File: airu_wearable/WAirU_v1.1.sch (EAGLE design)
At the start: 54 parts, among them Q2 MMBT3904LT1G, Q3 MMBT3904LT1G, Q4 BSS84, Q6 BSS84, U2 CN3065-DFN8, U3 HDC1080DMBT, U4 PAM2305AABADJ, U6 PAM2401, U7 ESP32_WROOM32_SKINNY

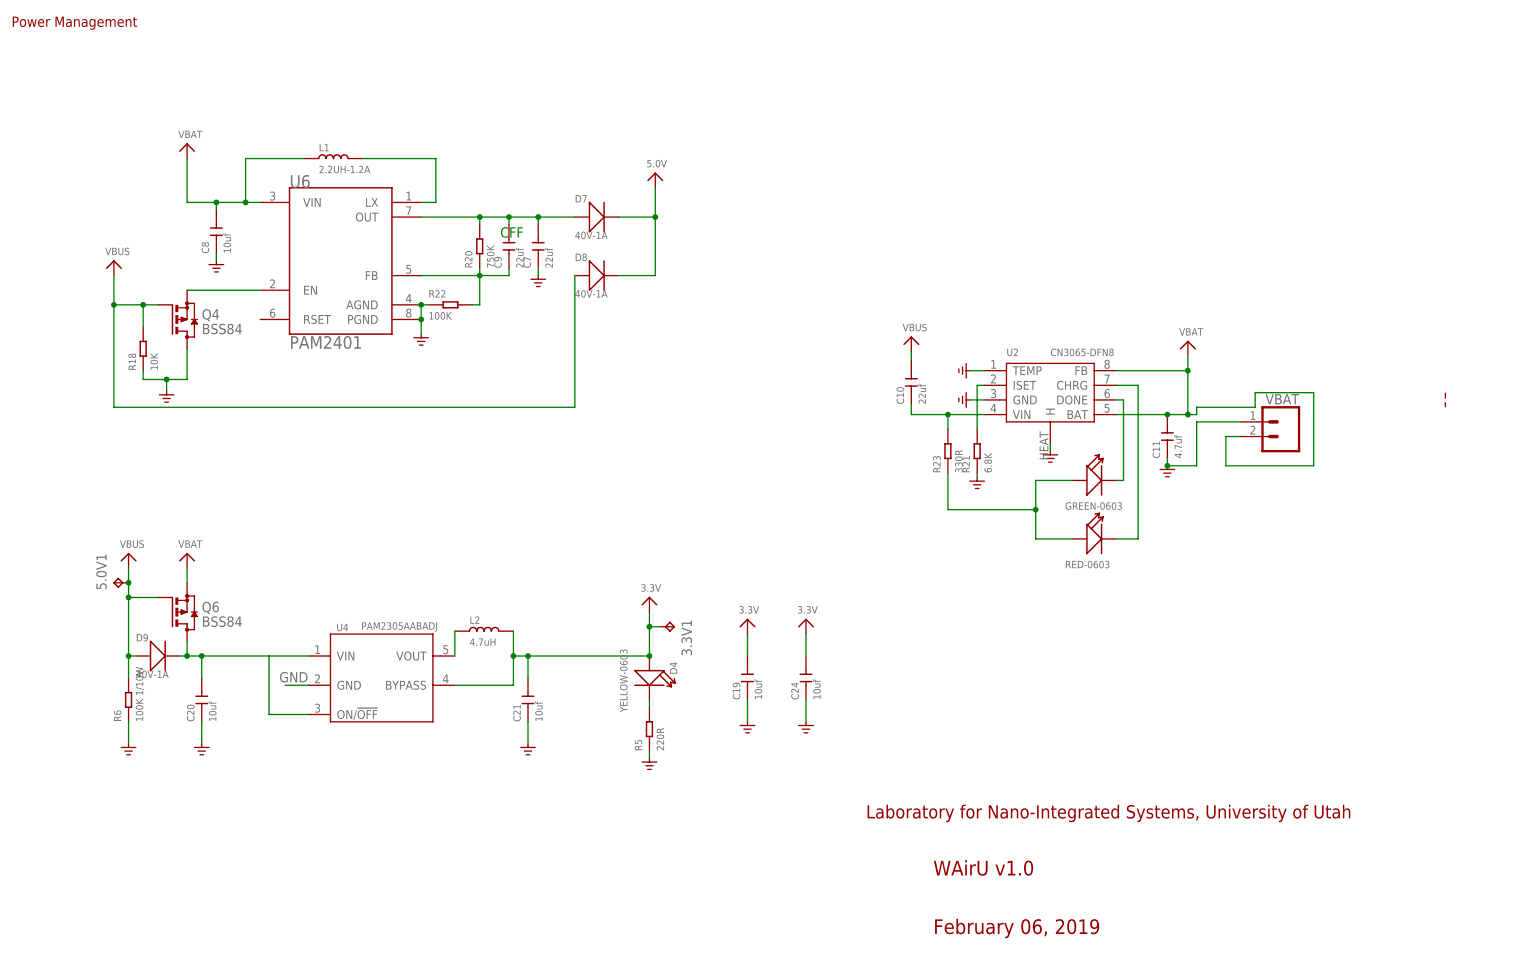
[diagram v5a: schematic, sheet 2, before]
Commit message: replaced LEDs with single LED, 5V and 3.3V buck/boost are now on the same VIN
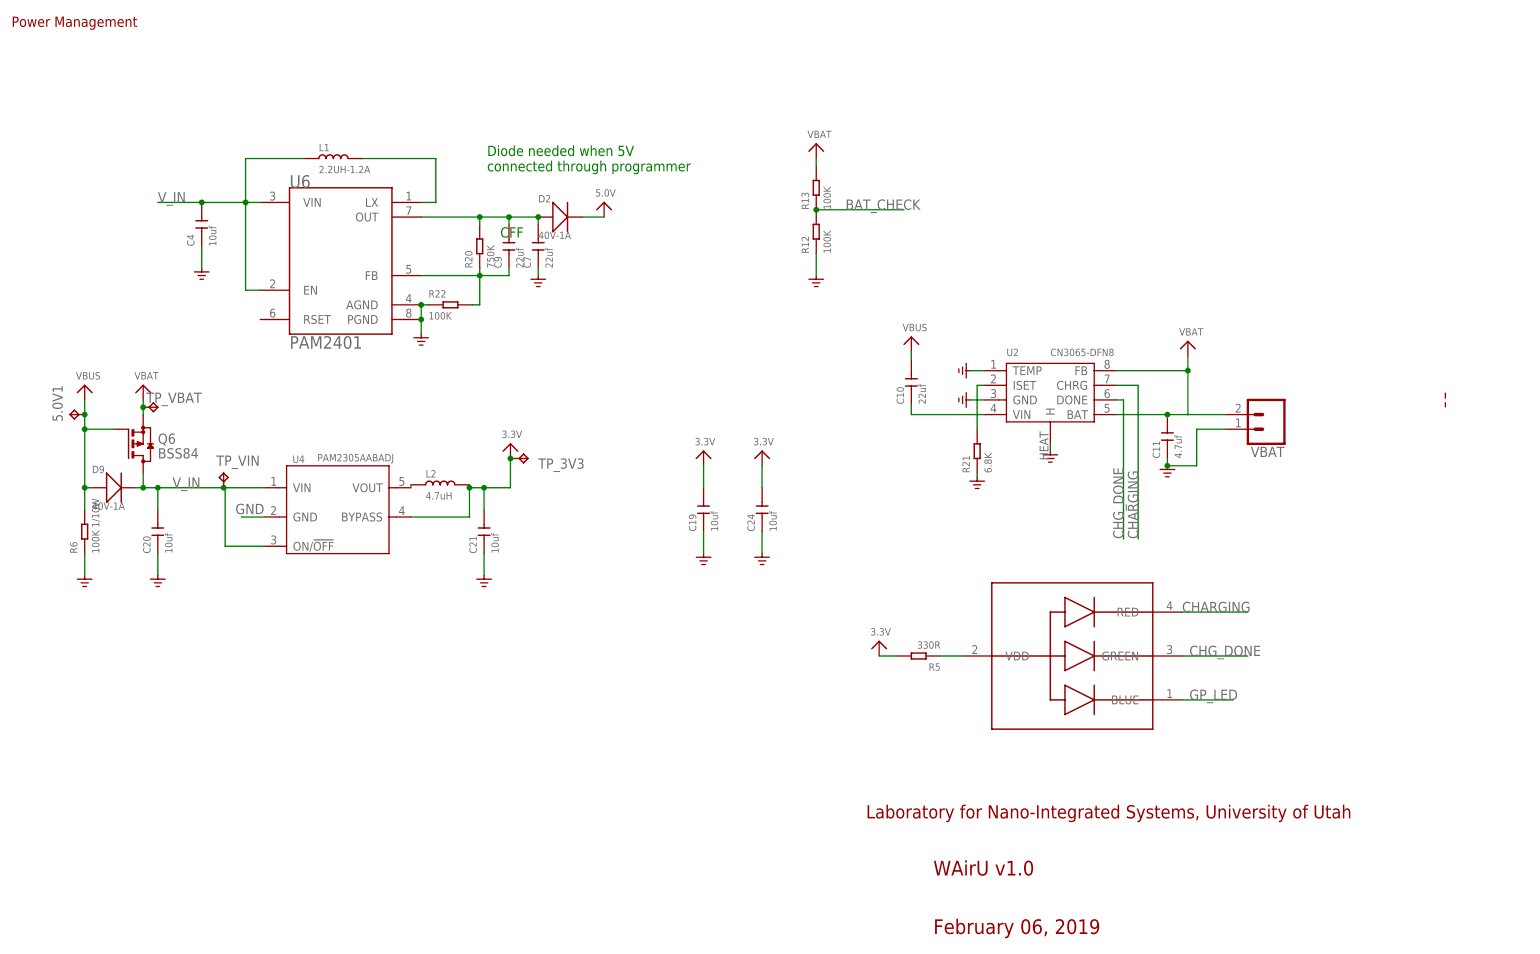
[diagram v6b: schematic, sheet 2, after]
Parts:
- removed 3.3V1: TPTP20SQ, testpad:TPTP20SQ
- removed 5: GREEN-0603, Seeed-LED:SMD-LED-CLEAR-GREEN(0603)
- removed 6, D1: RED-0603, Seeed-LED:LED-SMD-RED-DIFFUSED(0603)
- removed C8: 10uf, OPL_Capacitor:CERAMIC-10UF-10V-10%-X5R(0603)
- removed D4: YELLOW-0603, Seeed-LED:SMD-LED-CLEAR-YELLOW(0603)
- removed D7, D8: 40V-1A, Seeed-Diode:SMD-DIODE-SCHOTTKY-40V-1A(DO-214AC)
- removed Q4: BSS84, BSS84:BSS84
- removed R14: 220R, Seeed-Resistor:SMD-RES-220R-5%-1/10W(0603)
- removed R18: 10K, Seeed-Resistor:SMD-RES-10K-1%-1/10W(0603)
- removed R23: 330R, Seeed-Resistor:SMD-RES-330R-1%-1/10W(0603)
- added C4: 10uf, Seeed-Capacitor:CERAMIC-10UF-10V-10%-X5R(0603)
- added D2: 40V-1A, Seeed-Diode:SMD-DIODE-SCHOTTKY-40V-1A(DO-214AC)
- added R12, R13: 100K, OPL_Resistor:SMD-RES-100K-5%-1/10W(0603)
- added TP_3V3, TP_VBAT, TP_VIN: TPTP20SQ, testpad:TPTP20SQ
- added U$4: 19-237A/BHR6GHC-M01/2T, SS_OPL_Unmade:19-237A/BHR6GHC-M01/2T
- R5: value 220R -> 330R; device Seeed-Resistor:SMD-RES-220R-5%-1/10W(0603) -> Seeed-Resistor:SMD-RES-330R-1%-1/10W(0603)
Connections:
- removed net N$11: 5.+, 6.+, R23.1
- removed net N$14: 5.-, U2.DONE
- removed net N$21: D4.-, R5.2
- removed net N$23: 6.-, U2.CHRG
- removed net N$7: D1.+, R14.1
- removed net N$75: C20.2, D9.-, Q6.D, U4.ON/!OFF, U4.VIN
- removed net STAT_LED1: R14.2, U7.IO21
- removed net STAT_LED2: U7.IO19
- removed net STAT_LED3: U7.IO18
- new net BAT_CHECK: R12.2, R13.1, U7.I35/A1_7
- new net CHARGING: U$4.RED, U2.CHRG
- new net CHG_DONE: U$4.GREEN, U2.DONE
- new net GP_LED: U$4.BLUE, U7.IO13/A2_4
- new net VBUS_RAW: L3.1, USB1.VBUS
- new net V_IN: C20.2, C4.2, D9.-, L1.1, Q6.D, TP_VIN.TP, U4.ON/!OFF, U4.VIN, U6.EN, U6.VIN
- net 3.3V: now also R5.2, TP_3V3.TP; no longer 3.3V1.TP, D4.+
- net 5.0V: now also D2.-; no longer D7.-, D8.-, L3.2
- net GND: now also C4.1, R12.1; no longer C8.1, D1.-, Q4.D, R18.1, R5.1
- net N$4: now also C7.2, C9.2, D2.+, R20.2, U6.OUT; no longer Q4.S, U6.EN
- net N$5: no longer R23.2
- net N$9: now also R5.1, U$4.VDD; no longer C7.2, C9.2, D7.+, R20.2, U6.OUT
- net VBAT: now also R13.2, TP_VBAT.TP; no longer C8.2, L1.1, U6.VIN
- net VBUS: now also L3.2; no longer D8.+, L3.1, Q4.G, R18.2, USB1.VBUS
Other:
- note added: "Diode needed when 5V connected through programmer"
- note added: "GPIOs 6-11 are ESP32 NOR FLASH pins. Dont use them."
- note added: "PM & Program"
- note added: "PMS-TX (UART2-RX)"
- note added: "PM_NC / UART0-TX"
- note added: "PM_RESET"
- note added: "PM_SET / UART0-RX"
- note added: "PROG-DTR"
- note added: "PROG-RTS"
- note removed: "GPIOs 6-11 are ESP32 flashing pins. Dont use them."
- note removed: "PM"
- note removed: "STATUS LEDs"
- moved on the sheet: 5.0V1, C19, C20, C21, C24, D9, L2, L3, Q6, R5, R6, U4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

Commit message: an airwire
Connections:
- new net N$7: U7.IO13/A2_4
- net GP_LED: now also U7.IO21; no longer U7.IO13/A2_4
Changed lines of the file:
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@@
 <net name="GP_LED" class="0">
+<segment>
+<wire x1="78.74" y1="86.36" x2="93.98" y2="86.36" width="0.1524" layer="91"/>
+<label x="81.28" y="86.36" size="1.778" layer="95"/>
+<pinref part="U7" gate="G$1" pin="IO21"/>
+</segment>
+</net>
+<net name="N$7" class="0">
 <segment>
 <pinref part="U7" gate="G$1" pin="IO13/A2_4"/>
 <wire x1="78.74" y1="104.14" x2="93.98" y2="104.14" width="0.1524" layer="91"/>
-<label x="82.55" y="104.14" size="1.778" layer="95"/>
 </segment>
 </net>
